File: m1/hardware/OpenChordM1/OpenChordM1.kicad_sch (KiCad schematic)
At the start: 20 parts, among them J1 USB4105-GF-A, J2 SJ1-3523N, J3 SJ1-3523N, SW1 SW_Gateron_LP, SW10 EVQ-PUA02K, SW11 EVQ-PUA02K, SW2 SW_Gateron_LP, SW3 SW_Gateron_LP, SW4 SW_Gateron_LP, SW5 SW_Gateron_LP, SW6 SW_Gateron_LP, SW7 SW_Gateron_LP, SW8 SW_Gateron_LP, SW9 EVQ-PUA02K, U1 RP2040, U2 CT_Slider_Chev_3_74d5_15_noESD, U3 IQS572-BL-QNR, U4 AT42QT2120-XUR, U5 CT_Trackpad_7x7_37D75

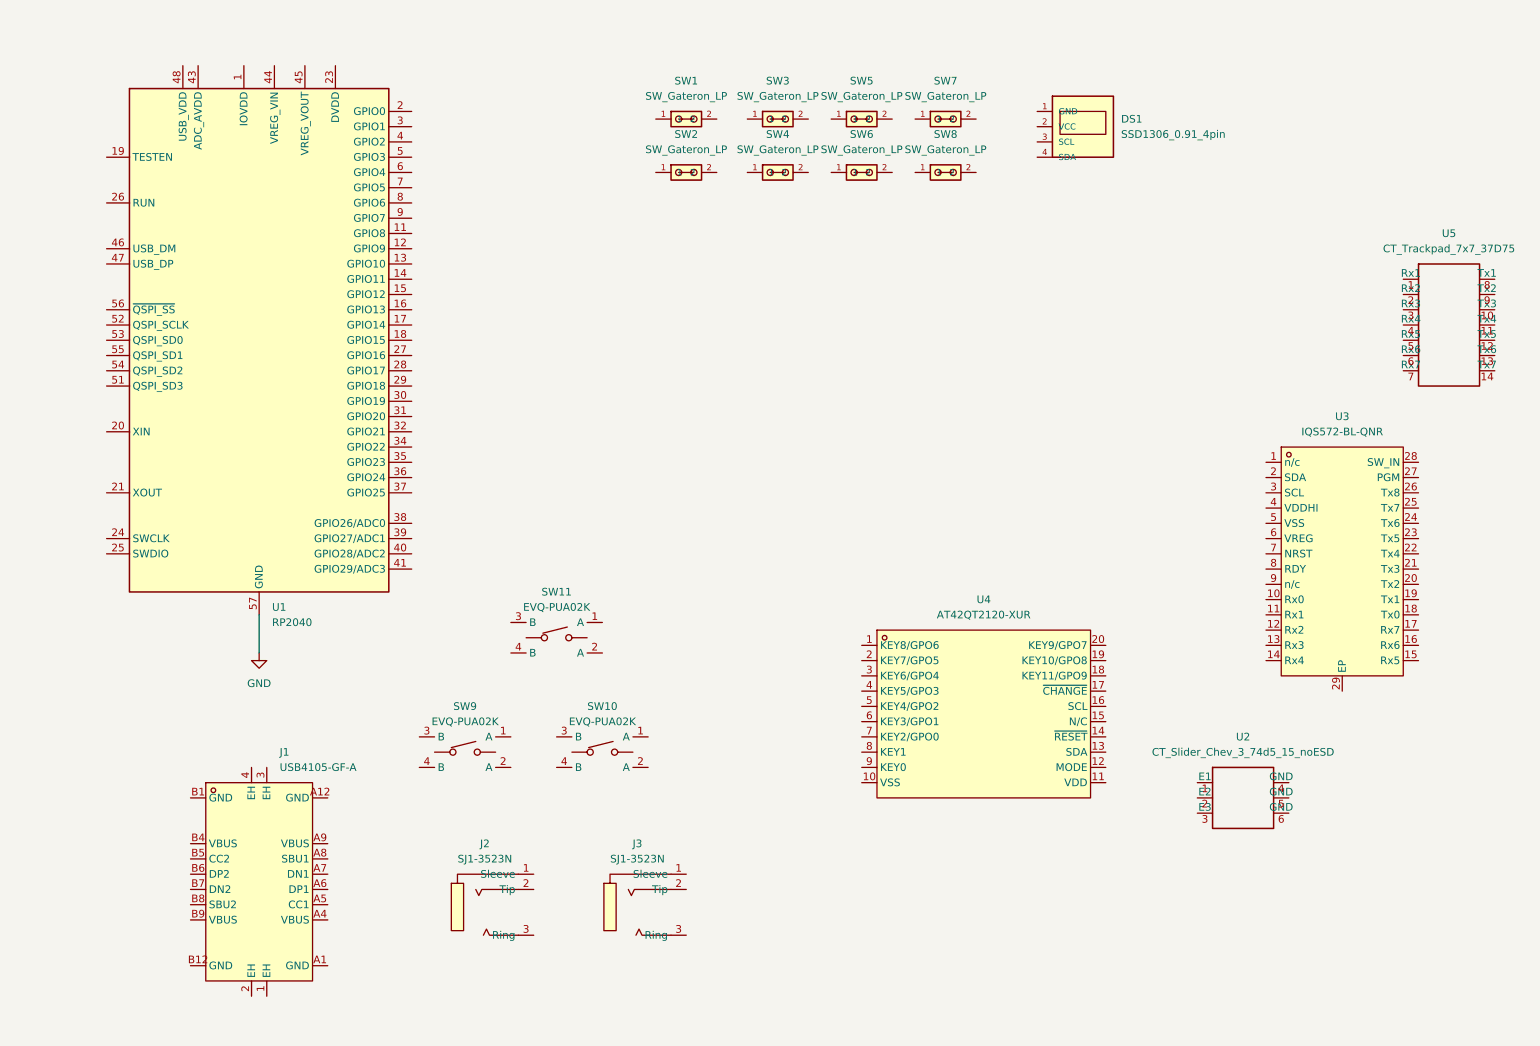
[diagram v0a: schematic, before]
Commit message: Lock M1 support BOM and add TLP2361 KiCad lib.
Document flash/crystal/LDO/ESD/MIDI IN recipe, replace H11L1 with TLP2361, and save current schematic/PCB progress before support-part placement.
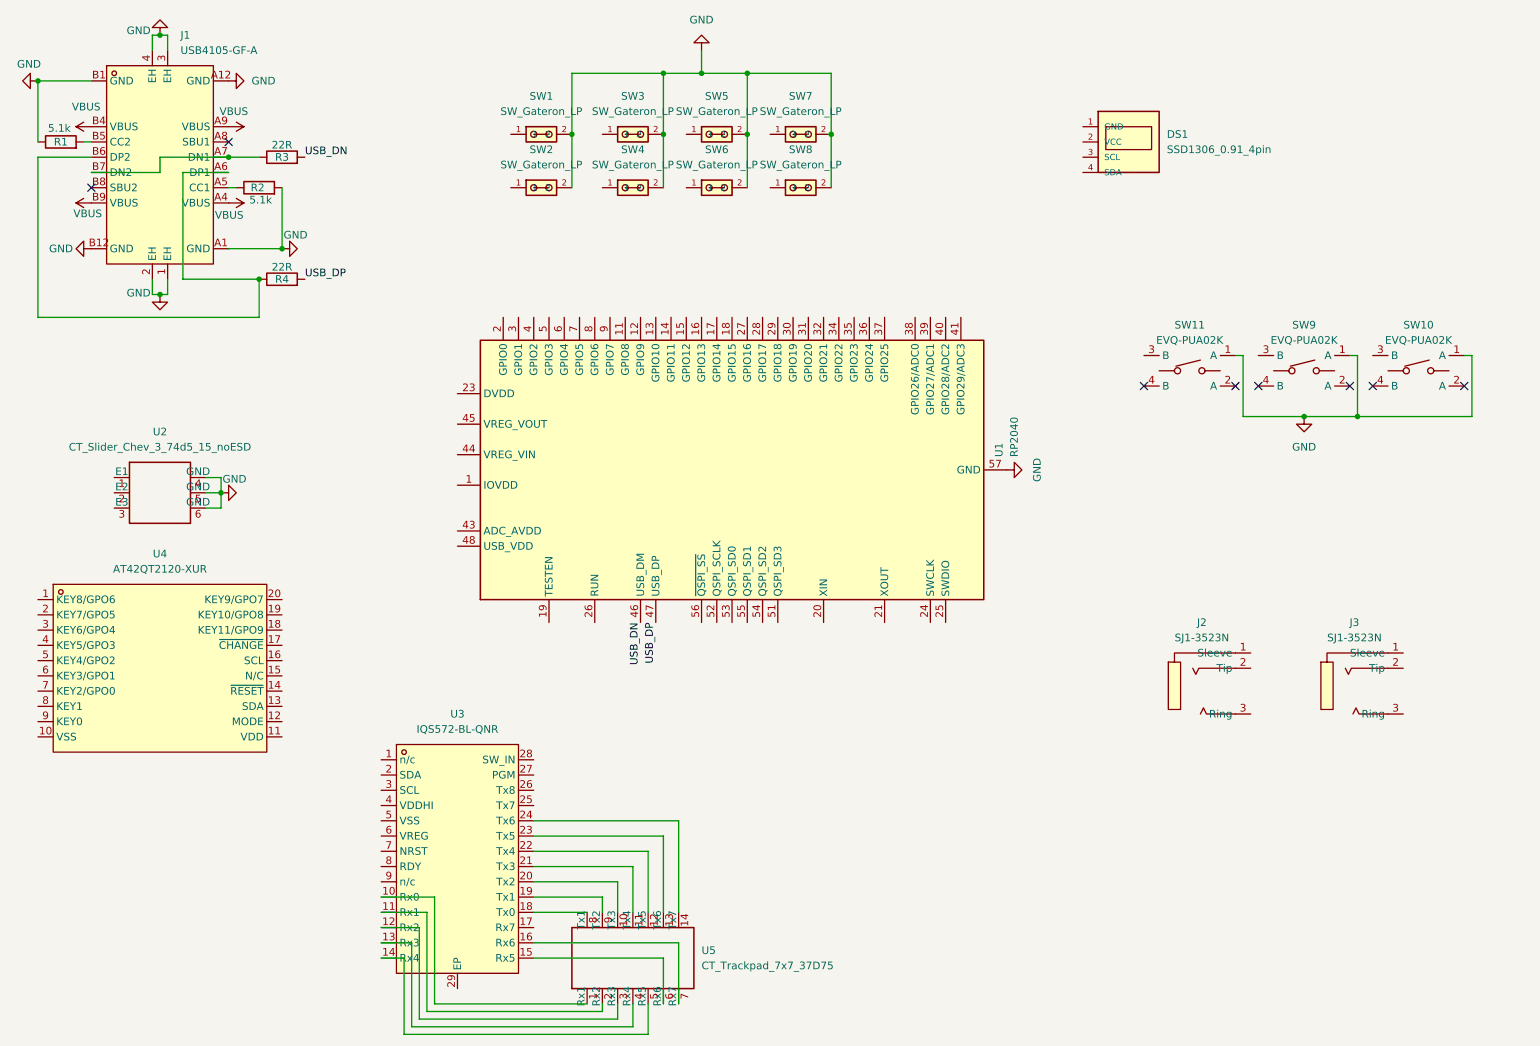
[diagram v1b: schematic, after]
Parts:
- added R1, R2: 5.1k, Inductor_SMD:L_CommonModeChoke_Coilcraft_0603USB, symbol Device:R
- added R3, R4: 22R, symbol Device:R
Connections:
- net GND: now also J1.1 (EH), J1.2 (EH), J1.3 (EH), J1.4 (EH), J1.A1 (GND), J1.A12 (GND), J1.B1 (GND), J1.B12 (GND), SW1.2, SW10.1 (A), SW11.1 (A), SW2.2, SW3.2, SW4.2, SW5.2, SW6.2, SW7.2, SW8.2, SW9.1 (A), U2.4 (GND), U2.5 (GND), U2.6 (GND), R1.1, R2.2
- net at U5.1 (Rx1): now also U3.10 (Rx0)
- net at U5.10 (Tx3): now also U3.20 (Tx2)
- net at U5.11 (Tx4): now also U3.21 (Tx3)
- net at U5.12 (Tx5): now also U3.22 (Tx4)
- net at U5.13 (Tx6): now also U3.23 (Tx5)
- net at U5.14 (Tx7): now also U3.24 (Tx6)
- net at U5.2 (Rx2): now also U3.11 (Rx1)
- net at U5.3 (Rx3): now also U3.12 (Rx2)
- net at U5.4 (Rx4): now also U3.13 (Rx3)
- net at U5.5 (Rx5): now also U3.14 (Rx4)
- net at U5.6 (Rx6): now also U3.15 (Rx5)
- net at U5.7 (Rx7): now also U3.16 (Rx6)
- net at U5.8 (Tx1): now also U3.18 (Tx0)
- net at U5.9 (Tx2): now also U3.19 (Tx1)
- net VBUS: now reaches J1.A4 (VBUS)
- net VBUS: now also J1.A9 (VBUS), J1.B4 (VBUS), J1.B9 (VBUS)
- net at J1.A5 (CC1): now also R2.1
- net at J1.A6 (DP1): now also J1.B6 (DP2), R4.1
- net at J1.A7 (DN1): now also J1.B7 (DN2), R3.1
- net at J1.B5 (CC2): now also R1.2
- net USB_DN: now reaches U1.46 (USB_DM)
- net USB_DN: now also R3.2
- net USB_DP: now reaches U1.47 (USB_DP)
- net USB_DP: now also R4.2
- no-connect marks 0 -> 8
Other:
- moved on the sheet: DS1, J1, J2, J3, SW1, SW10, SW11, SW2, SW3, SW4, SW5, SW6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
